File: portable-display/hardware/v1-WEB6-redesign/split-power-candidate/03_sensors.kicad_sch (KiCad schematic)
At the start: 19 parts, among them Q1 2N7002, Q2 2N7002, U4 LIS2DW12TR, U5 RV-3028-C7, U6 SN74LVC1G123DCTR

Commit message: fix(hardware): extend automatic wake pulse to nominal 3 seconds
Use a 910k resistor and 3.3uF 0805 timing capacitor, bind JLCPCB parts, and reroute the timing nets. Synchronize schematics, local footprint and independent component requirements. Physical timing and retrigger behavior remain subject to validation.
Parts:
- C23: value 100n -> 3.3u; footprint Sameat:0402 -> Sameat:C_0805_2012Metric; symbol Sameat:C23_100n -> Sameat:C23_3.3u; LCSC (none) -> C7393948; MPN (none) -> TCC0805X7R335K250FT
- R12: value 820k -> 910k; symbol Sameat:R12_820k -> Sameat:R12_910k; LCSC (none) -> C352384; MPN (none) -> AECR0402F910KK9
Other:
- note added: "WAKE TIMER: R12 910k 1%; C23 3.3uF 25V X7R 10% 0805; approx 3 s nominal. Measure PWRON_N LOW for 2.2-3.8 s. RC tolerances alone do NOT guarantee this window. Use latched active-low interrupts; repeated edges retrigger U6. See WAKE_PULSE_REPAIR_CN.md."
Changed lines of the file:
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@@
 	(title_block
 		(title "03 Always-on Sensors / Wake")
-		(date "2026-09-24")
-		(rev "LCD-IO1")
+		(date "2026-10-01")
+		(rev "WAKE1")
 		(company "Sameat")
 		(comment 1 "Current PCB pin nets; C3036461 factory configuration NOT verified")
@@
 	)
 	(symbol
-		(lib_id "Sameat:C23_100n")
+		(lib_id "Sameat:C23_3.3u")
 		(at 63.500 139.700 0)
 		(unit 1)
@@
 			)
 		)
-		(property "Value" "100n"
+		(property "Value" "3.3u"
 			(at 63.500 132.620 0)
 			(effects
@@
 			)
 		)
-		(property "Footprint" "Sameat:0402"
+		(property "Footprint" "Sameat:C_0805_2012Metric"
 			(at 63.500 139.700 0)
 			(effects
@@
 			)
 		)
-		(property "Datasheet" ""
+		(property "Datasheet" "https://jlcpcb.com/partdetail/CCTC-TCC0805X7R335K250FT/C7393948"
 			(at 63.500 139.700 0)
 			(effects
@@
 			)
 		)
-		(property "MPN" ""
+		(property "MPN" "TCC0805X7R335K250FT"
 			(at 63.500 139.700 0)
 			(effects
@@
 			)
 		)
-		(property "LCSC" ""
+		(property "LCSC" "C7393948"
 			(at 63.500 139.700 0)
 			(effects
@@
 			)
 		)
-		(property "Description" ""
+		(property "Description" "Wake timing capacitor: 3.3uF 25V X7R 10% 0805; bias/temperature timing qualification required"
 			(at 63.500 139.700 0)
 			(effects
@@
 	)
 	(symbol
-		(lib_id "Sameat:R12_820k")
+		(lib_id "Sameat:R12_910k")
 		(at 327.660 163.830 0)
 		(unit 1)
@@
 			)
 		)
-		(property "Value" "820k"
+		(property "Value" "910k"
 			(at 327.660 156.750 0)
 			(effects
@@
 			)
 		)
-		(property "Datasheet" ""
+		(property "Datasheet" "https://jlcpcb.com/partdetail/RESI-AECR0402F910KK9/C352384"
 			(at 327.660 163.830 0)
 			(effects
@@
 			)
 		)
-		(property "MPN" ""
+		(property "MPN" "AECR0402F910KK9"
 			(at 327.660 163.830 0)
 			(effects
@@
 			)
 		)
-		(property "LCSC" ""
+		(property "LCSC" "C352384"
 			(at 327.660 163.830 0)
 			(effects
@@
 			)
 		)
-		(property "Description" ""
+		(property "Description" "Wake timer: 910k 1% 0402; with C23 3.3u approx 3s, measure 2.2-3.8s"
 			(at 327.660 163.830 0)
 			(effects
@@
 	)
 	(embedded_fonts no)
+	(text "WAKE TIMER: R12 910k 1%; C23 3.3uF 25V X7R 10% 0805; approx 3 s nominal.\nMeasure PWRON_N LOW for 2.2-3.8 s. RC tolerances alone do NOT guarantee this window.\nUse latched active-low interrupts; repeated edges retrigger U6. See WAKE_PULSE_REPAIR_CN.md."
+		(at 38.1 370.84 0)
+		(effects
+			(font
+				(size 1.27 1.27)
+			)
+			(justify left)
+		)
+	)
 )

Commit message: feat: add split power candidate hardware design and wake domain verification reports
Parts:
- added C52: 100n, Sameat:0402, symbol Sameat:C52_100n
- added U11: SN74LVC2G17DBVR, Sameat:SN74LVC2G17_DBV6, symbol Sameat:U11_SN74LVC2G17DBVR
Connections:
- net 3V3: now also C52.1, U11.5 (VCC); no longer R17.1, R18.1
- net ACCEL_INT_N: now also U11.3 (2A)
- net GND: now also C52.2, U11.2 (GND)
- net RTC_3V3: now also R17.1, R18.1
- net RTC_INT_N: now also U11.1 (1A)
- new net ACCEL_INT_SOC_N: U11.4 (2Y)
- new net RTC_INT_SOC_N: U11.6 (1Y)
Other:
- note added: "WAKE DOMAINS: R17/R18 pull up to RTC_3V3. U11 SN74LVC2G17 isolates both IRQs from U2. U11/C52 use switched 3V3. RTC_INT_SOC_N -> PE7; ACCEL_INT_SOC_N -> PE6; polarity unchanged. Require latched active-low IRQs and AON supply retention. See WAKE_DOMAIN_REPAIR_CN.md."
- moved on the sheet: C23, C24, C25, C26, D2, D3, Q1, Q2, R11, R12, R13, R14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

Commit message: fix(sch): regenerate candidate schematic with R33/R34 FEL recovery on PC1
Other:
- moved on the sheet: C23, C52, D2, R11, R12, R13, R14, R16, R17

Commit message: fix(pcb): add C53 1uF (C52923) + C54 100nF (C1525) at U8 TPS22918 VIN
Both JLC basic 0402, F.Cu, GND via outside pad (>=0.15 mm pad-to-hole).
Schematic regenerated; DRC/parity/ERC 0.
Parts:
- added C53: 1u, Sameat:0402, symbol Sameat:C53_1u
- added C54: 100n, Sameat:0402, symbol Sameat:C54_100n
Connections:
- net 3V3: now also C53.1, C54.1
- net GND: now also C53.2, C54.2
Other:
- moved on the sheet: C23, C25, C26, C52, D2, R11, R12, R13, R14, R16, R17

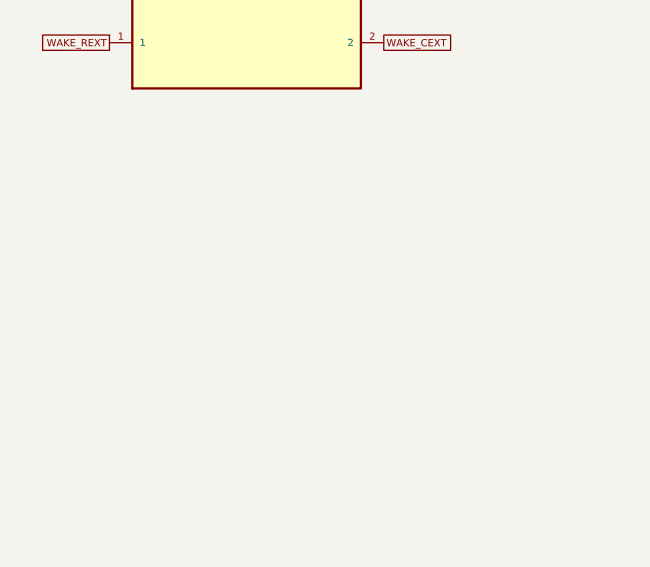
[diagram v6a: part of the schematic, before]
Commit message: feat(j5): swap microSD to in-stock XKTF-0803-0, TPD4E05U06 flow-through ESD, reroute SD bus off Y1
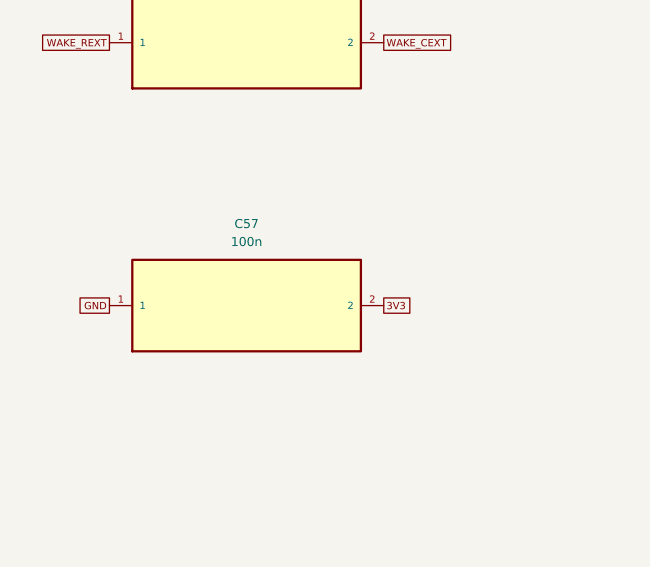
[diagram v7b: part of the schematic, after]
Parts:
- added C57: 100n, Sameat:0402, symbol Sameat:C57_100n
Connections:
- net 3V3: now also C57.2
- net GND: now also C57.1
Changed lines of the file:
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@@
+		)
+	)
+	(symbol
+		(lib_id "Sameat:C57_100n")
+		(at 63.500 198.120 0)
+		(unit 1)
+		(exclude_from_sim no)
+		(in_bom yes)
+		(on_board yes)
+		(dnp no)
+		(property "Reference" "C57"
+			(at 63.500 189.040 0)
+			(effects
+				(font
+					(size 1 1)
+				)
+			)
+		)
+		(property "Value" "100n"
+			(at 63.500 191.040 0)
+			(effects
+				(font
+					(size 1 1)
+				)
+			)
+		)
+		(property "Footprint" "Sameat:0402"
+			(at 63.500 198.120 0)
+			(effects
+				(font
+					(size 1 1)
+				)
+				(hide yes)
+			)
+		)
+		(property "Datasheet" ""
+			(at 63.500 198.120 0)
+			(effects
+				(font
+					(size 1 1)
+				)
+				(hide yes)
+			)
+		)
+		(property "MPN" "CL05B104KO5NNNC"
+			(at 63.500 198.120 0)
+			(effects
+				(font
+					(size 1 1)
+				)
+				(hide yes)
+			)
+		)
+		(property "LCSC" "C1525"
+			(at 63.500 198.120 0)
+			(effects
+				(font
+					(size 1 1)
+				)
+				(hide yes)
+			)
+		)
+		(property "Description" ""
+			(at 63.500 198.120 0)
+			(effects
+				(font
+					(size 1 1)
+				)
+				(hide yes)
+			)
+		)
+		(pin "1"
+		)
+		(pin "2"
+		)
+		(instances
+			(project "ak_display_38x64_SPLIT_POWER_CANDIDATE"
+				(path "/b7613259-1701-5a92-a5a3-2c5d87fd6070/51072dd9-1bb1-5c78-ad53-b3e9d0a07bc6"
+					(reference "C57")
+					(unit 1)
+				)
+			)
+		)
+	)
+	(global_label "GND"
+		(shape passive)
+		(at 48.260 198.120 180)
+		(effects
+			(font
+				(size .8 .8)
+			)
+			(justify right)
+		)
+	)
+	(global_label "3V3"
+		(shape passive)
+		(at 78.740 198.120 0)
+		(effects
+			(font
+				(size .8 .8)
+			)
+			(justify left)
 		)
 	)

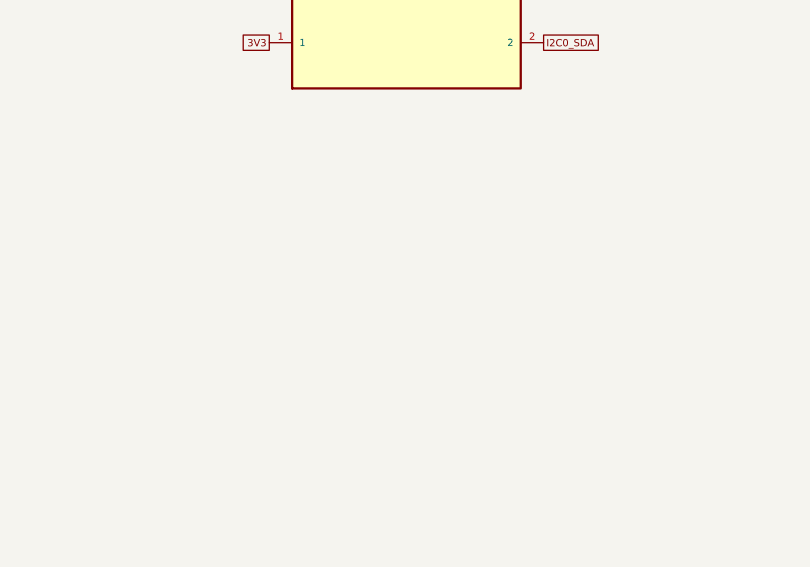
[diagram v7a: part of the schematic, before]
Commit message: fix(power): feed U10 TPS65631 from 3V3 via local In2 taps; 2x10u+100n under U10
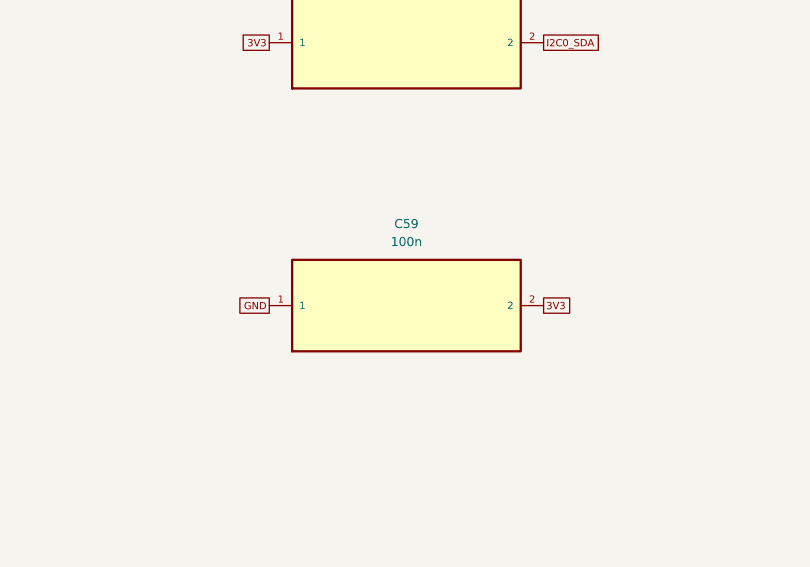
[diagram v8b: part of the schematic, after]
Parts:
- added C59: 100n, Sameat:0402, symbol Sameat:C59_100n
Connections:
- net 3V3: now also C59.2
- net GND: now also C59.1
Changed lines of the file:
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@@
+		)
+	)
+	(symbol
+		(lib_id "Sameat:C59_100n")
+		(at 195.580 222.250 0)
+		(unit 1)
+		(exclude_from_sim no)
+		(in_bom yes)
+		(on_board yes)
+		(dnp no)
+		(property "Reference" "C59"
+			(at 195.580 213.170 0)
+			(effects
+				(font
+					(size 1 1)
+				)
+			)
+		)
+		(property "Value" "100n"
+			(at 195.580 215.170 0)
+			(effects
+				(font
+					(size 1 1)
+				)
+			)
+		)
+		(property "Footprint" "Sameat:0402"
+			(at 195.580 222.250 0)
+			(effects
+				(font
+					(size 1 1)
+				)
+				(hide yes)
+			)
+		)
+		(property "Datasheet" ""
+			(at 195.580 222.250 0)
+			(effects
+				(font
+					(size 1 1)
+				)
+				(hide yes)
+			)
+		)
+		(property "MPN" "CL05B104KO5NNNC"
+			(at 195.580 222.250 0)
+			(effects
+				(font
+					(size 1 1)
+				)
+				(hide yes)
+			)
+		)
+		(property "LCSC" "C1525"
+			(at 195.580 222.250 0)
+			(effects
+				(font
+					(size 1 1)
+				)
+				(hide yes)
+			)
+		)
+		(property "Description" ""
+			(at 195.580 222.250 0)
+			(effects
+				(font
+					(size 1 1)
+				)
+				(hide yes)
+			)
+		)
+		(pin "1"
+		)
+		(pin "2"
+		)
+		(instances
+			(project "ak_display_38x64_SPLIT_POWER_CANDIDATE"
+				(path "/b7613259-1701-5a92-a5a3-2c5d87fd6070/51072dd9-1bb1-5c78-ad53-b3e9d0a07bc6"
+					(reference "C59")
+					(unit 1)
+				)
+			)
+		)
+	)
+	(global_label "GND"
+		(shape passive)
+		(at 180.340 222.250 180)
+		(effects
+			(font
+				(size .8 .8)
+			)
+			(justify right)
+		)
+	)
+	(global_label "3V3"
+		(shape passive)
+		(at 210.820 222.250 0)
+		(effects
+			(font
+				(size .8 .8)
+			)
+			(justify left)
 		)
 	)
